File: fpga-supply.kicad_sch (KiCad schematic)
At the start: 70 parts, among them U1 MPFS250T-FCVG484, Y3 Oscillator_125MHz_DSC1103DI2, Y5 Oscillator_50MHz_ECS_1612MV

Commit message: [#57505] Start reworking schematic to hierarchical structure
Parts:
- removed C2, C4: C_100n_0402, antmicro-footprints:C_0402_1005Metric, symbol antmicroCapacitors0402:C_100n_0402
- removed R60, R87: R_0R_0402, antmicro-footprints:R_0402_1005Metric, symbol antmicroResistors0402:R_0R_0402
- removed unit 2 of U1
- removed unit 1 of U1
- removed Y3: Oscillator_125MHz_DSC1103DI2, antmicro-footprints:Oscillator_SMD_Microchip_DSC1103DI2_2.5x2x0.85mm, symbol antmicroOscillators:Oscillator_125MHz_DSC1103DI2
- removed Y5: Oscillator_50MHz_ECS_1612MV, antmicro-footprints:Oscillator_SMD_ECS_1612MV_1.6x1.2x0.6mm, symbol antmicroOscillators:Oscillator_50MHz_ECS_1612MV
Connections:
- no-connect marks 49 -> 0
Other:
- note removed: "2-lane CSI works only when VDDI = 1V8"
- note removed: "PolarFire Bank 0 HSIO"
- note removed: "PolarFire Bank 1 GPIO"
- note removed: "PolarFire clocks"

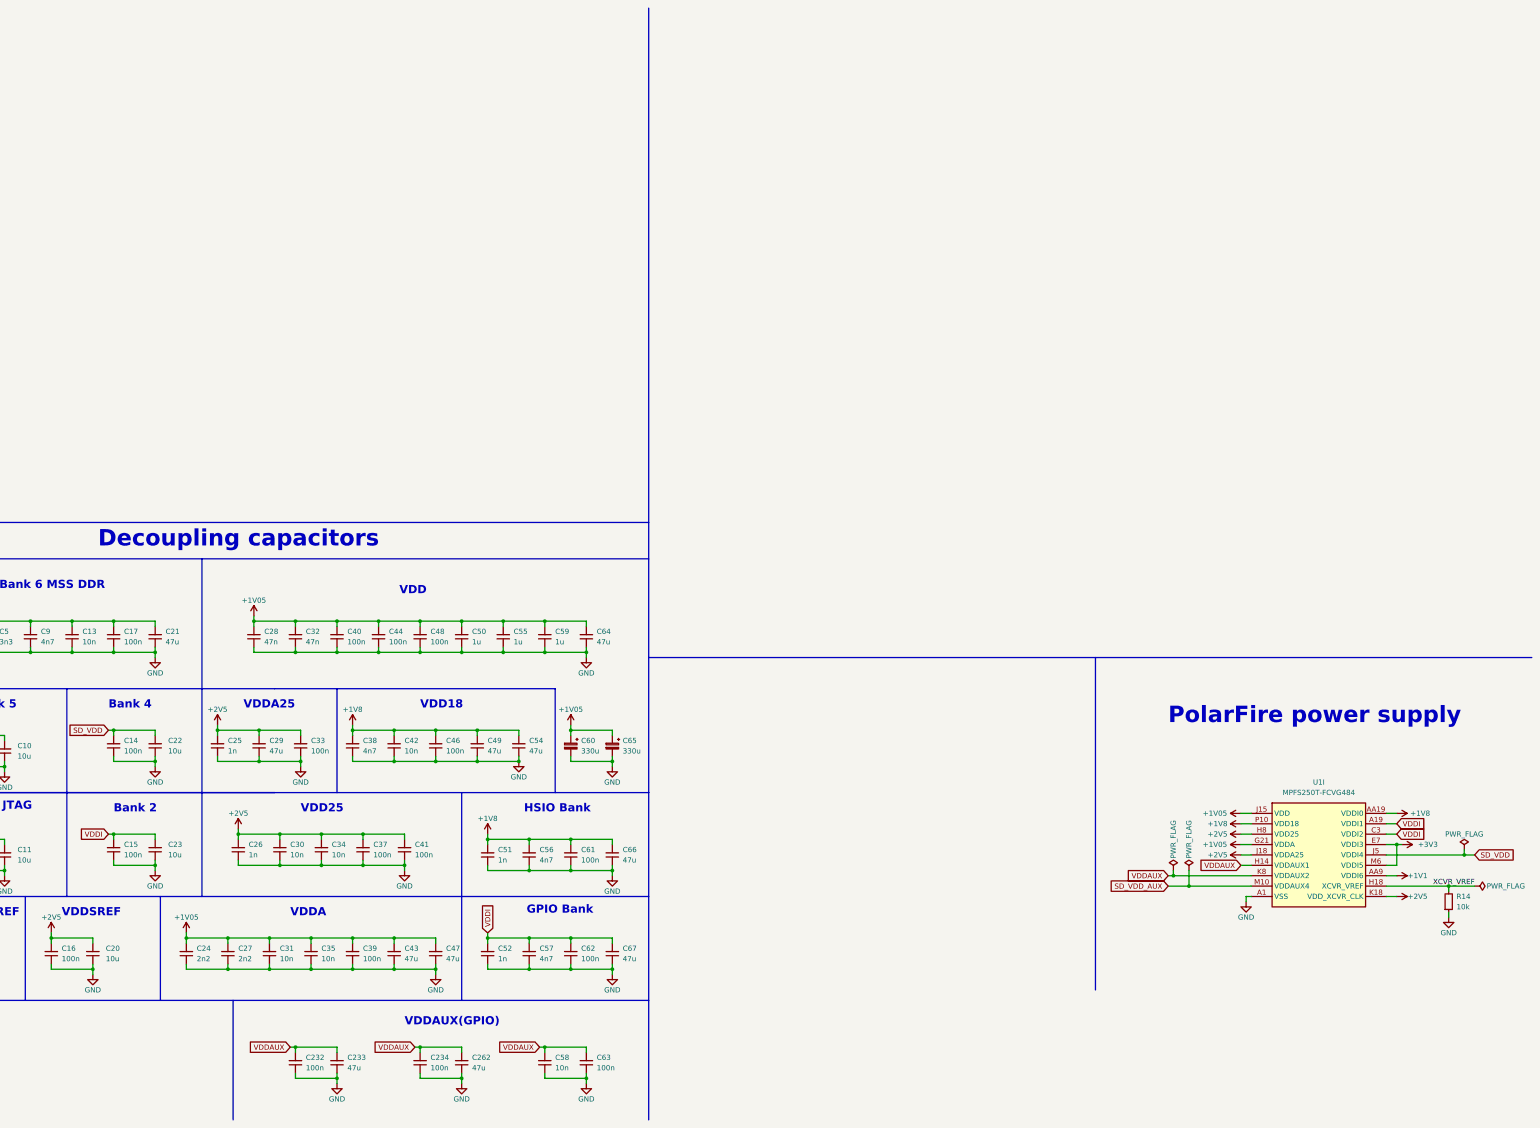
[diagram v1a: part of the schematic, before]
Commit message: [#57505] Continue migration to hierarchical schematic
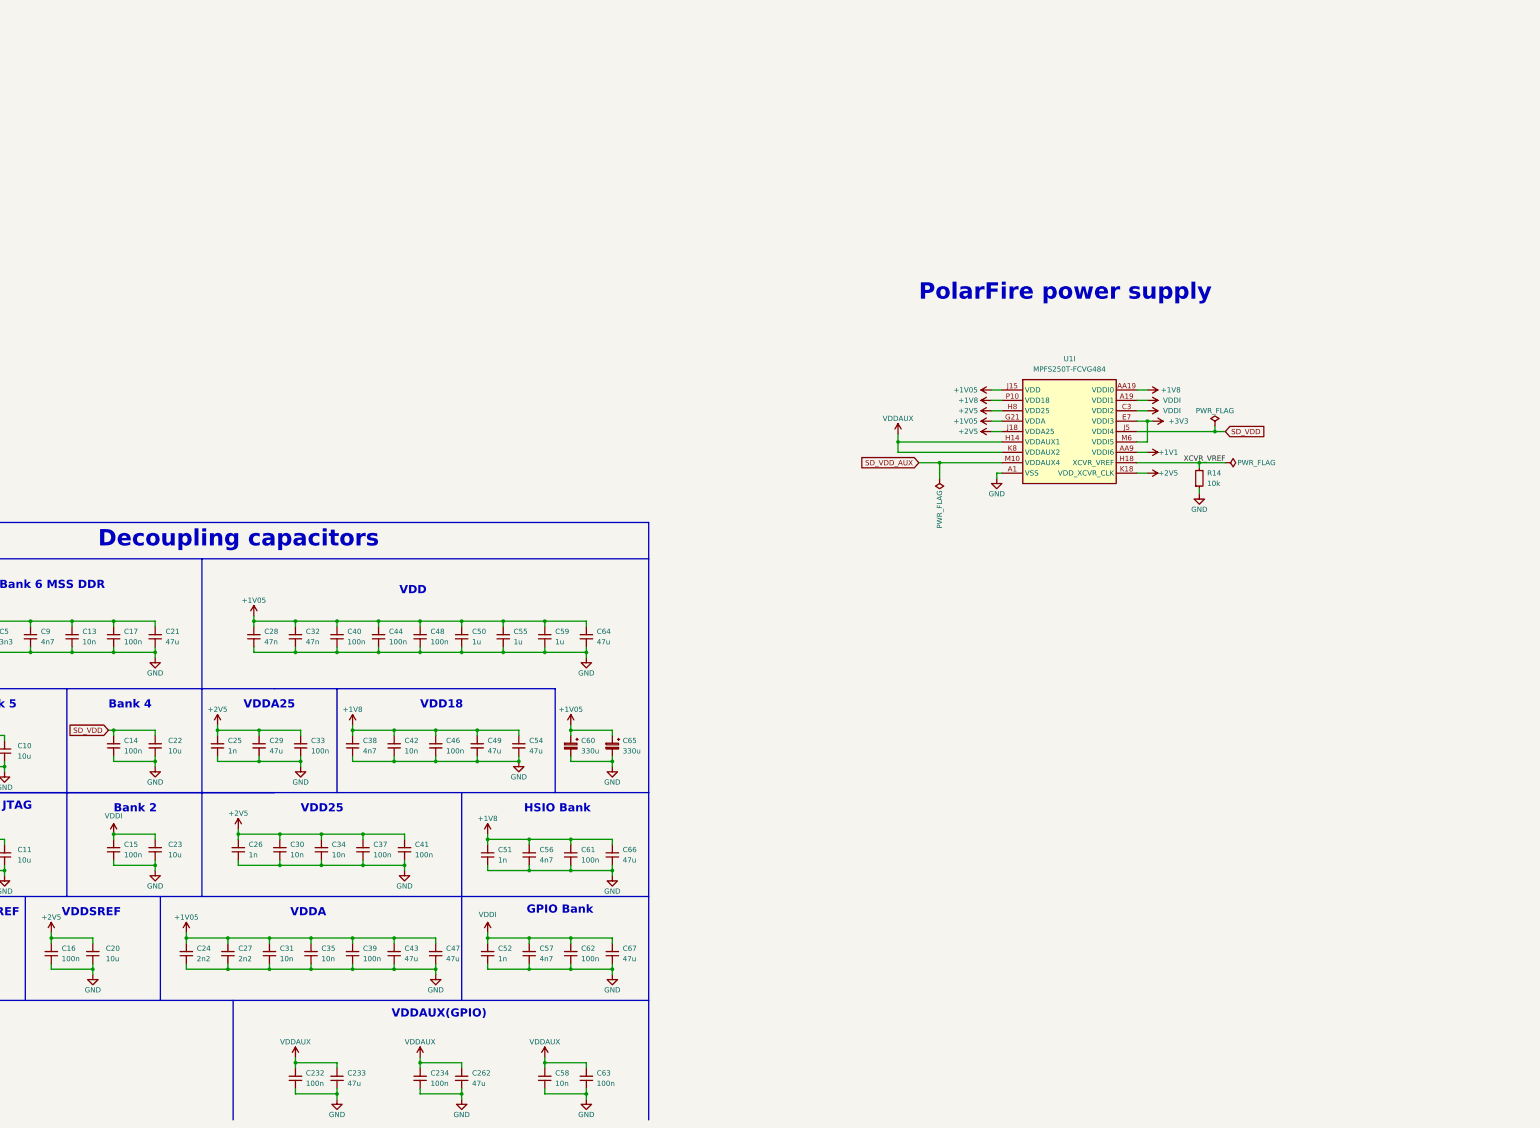
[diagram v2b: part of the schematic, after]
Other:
- moved on the sheet: C232, C233, C234, C262, C58, C63, R14, U1I

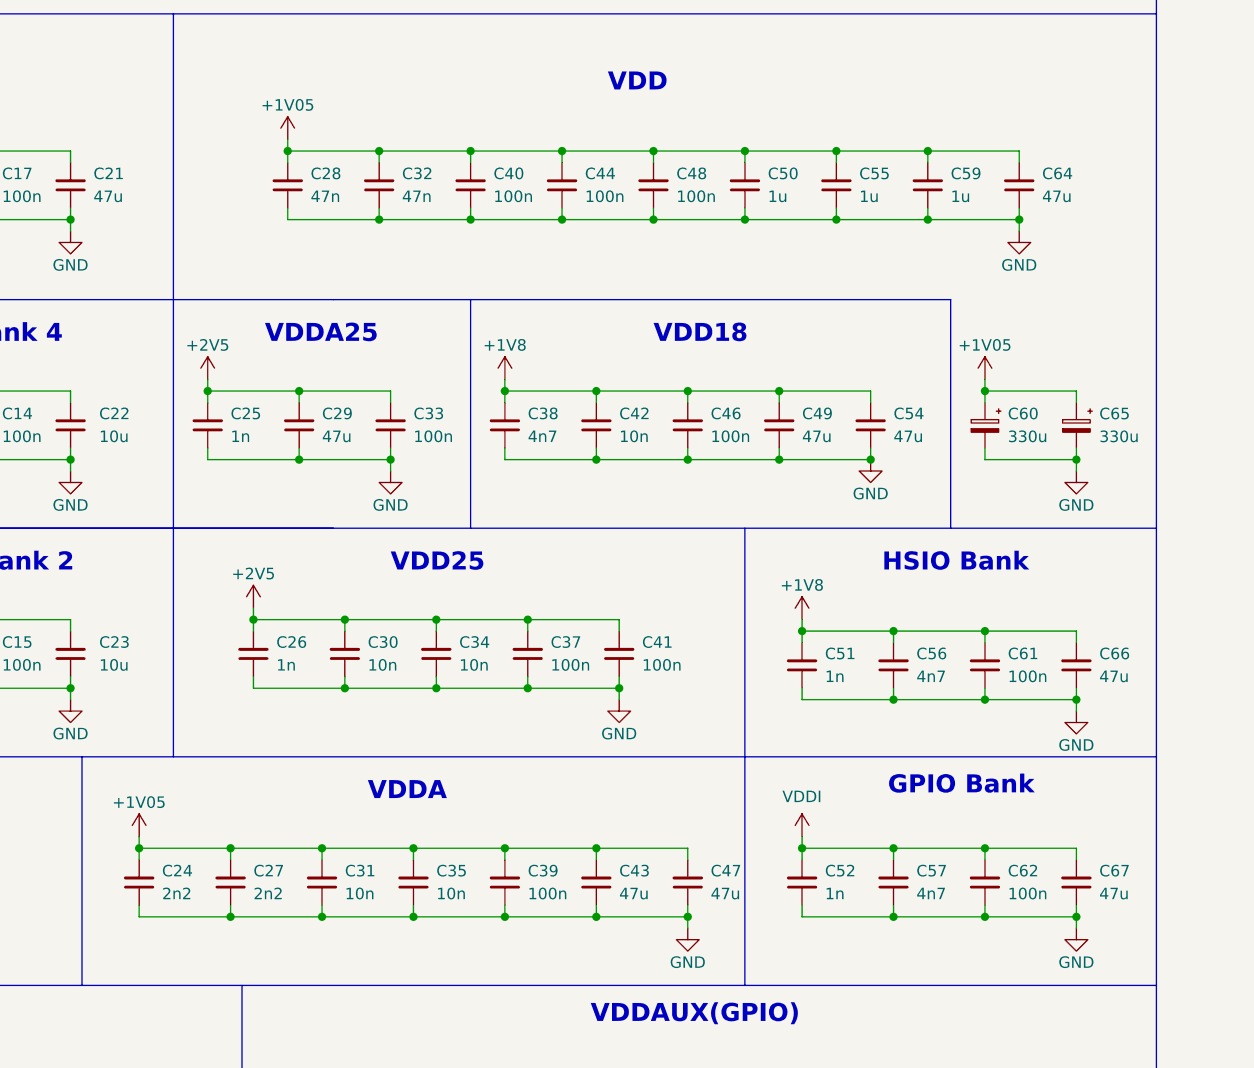
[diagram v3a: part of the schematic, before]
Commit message: [#57422] Update capacitor values
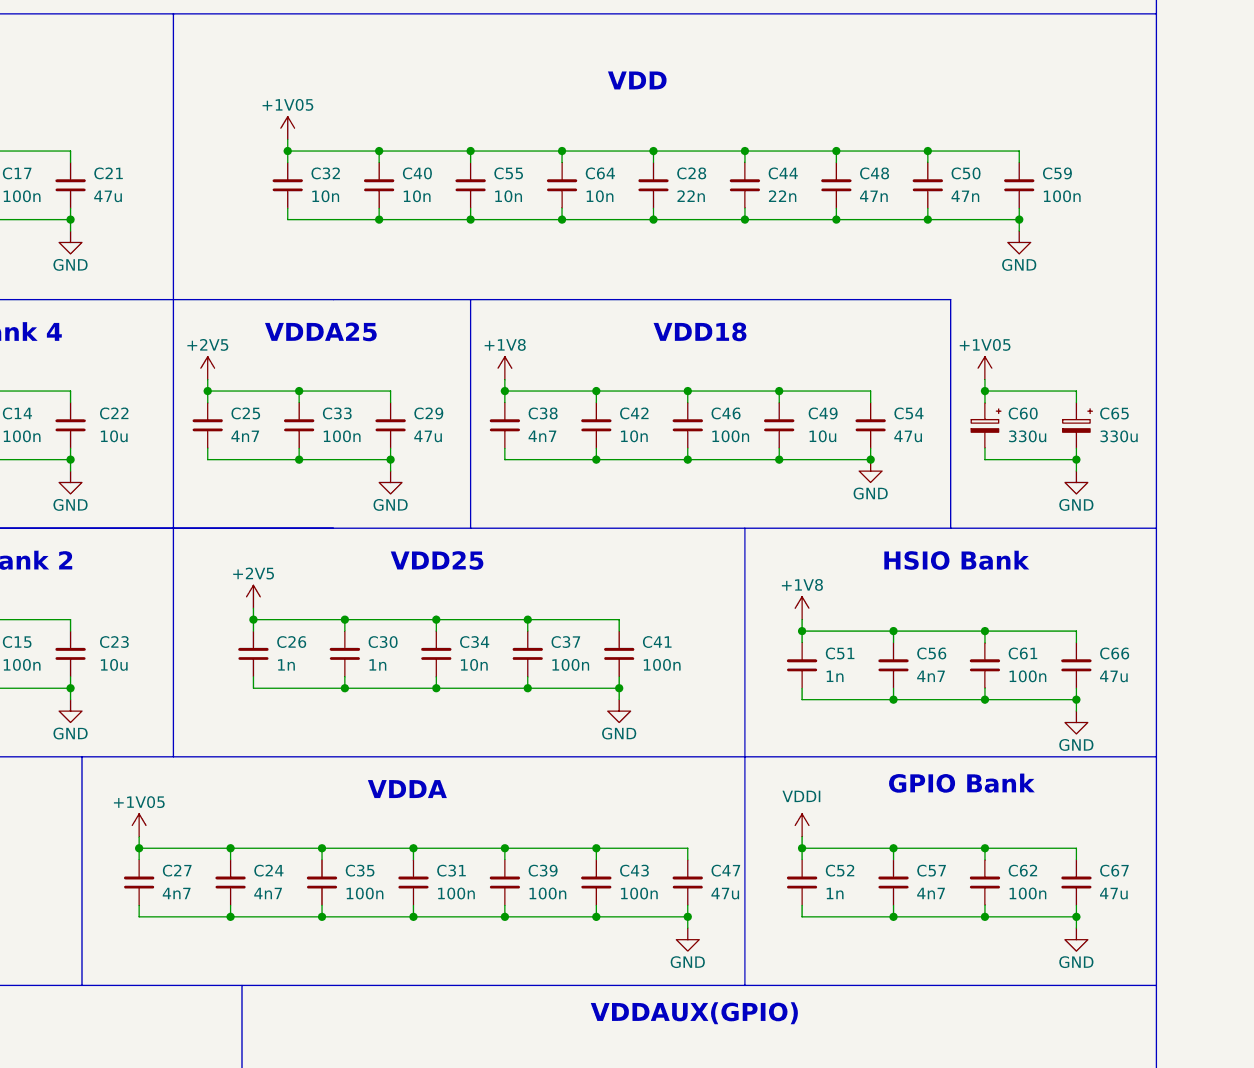
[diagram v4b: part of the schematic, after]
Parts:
- removed C24, C27: C_2n2_0402, antmicro-footprints:C_0402_1005Metric, symbol antmicroCapacitors0402:C_2n2_0402
- removed C25: C_1n_0402, antmicro-footprints:C_0402_1005Metric, symbol antmicroCapacitors0402:C_1n_0402
- removed C28, C32: C_47n_0402, antmicro-footprints:C_0402_1005Metric, symbol antmicroCapacitors0402:C_47n_0402
- removed C30, C31, C35: C_10n_0402, antmicro-footprints:C_0402_1005Metric, symbol antmicroCapacitors0402:C_10n_0402
- removed C40, C44, C48: C_100n_0402, antmicro-footprints:C_0402_1005Metric, symbol antmicroCapacitors0402:C_100n_0402
- removed C43, C49, C64: C_47u_0603, antmicro-footprints:C_0603_1608Metric, symbol antmicroCapacitors0603:C_47u_0603
- removed C50, C55, C59: C_1u_0402, antmicro-footprints:C_0402_1005Metric, symbol antmicroCapacitors0402:C_1u_0402
- added C24, C25, C27: C_4n7_0402, antmicro-footprints:C_0402_1005Metric, symbol antmicroCapacitors0402:C_4n7_0402
- added C28, C44: C_22n_0402, antmicro-footprints:C_0402_1005Metric, symbol antmicroCapacitors0402:C_22n_0402
- added C30: C_1n_0402, antmicro-footprints:C_0402_1005Metric, symbol antmicroCapacitors0402:C_1n_0402
- added C31, C35, C43, C59: C_100n_0402, antmicro-footprints:C_0402_1005Metric, symbol antmicroCapacitors0402:C_100n_0402
- added C32, C40, C55, C64: C_10n_0402, antmicro-footprints:C_0402_1005Metric, symbol antmicroCapacitors0402:C_10n_0402
- added C48, C50: C_47n_0402, antmicro-footprints:C_0402_1005Metric, symbol antmicroCapacitors0402:C_47n_0402
- added C49: C_10u_0402, antmicro-footprints:C_0402_1005Metric, symbol antmicroCapacitors0402:C_10u_0402
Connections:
- net +1V05: now also C24.2, C27.2, C28.2, C31.2, C32.2, C35.2, C40.2, C43.2, C44.2, C48.2, C50.2, C55.2, C59.2, C64.2
- net +1V8: now also C49.2
- net +2V5: now also C25.2, C30.2
- net GND: now also C24.1, C25.1, C27.1, C28.1, C30.1, C31.1, C32.1, C35.1, C40.1, C43.1, C44.1, C48.1, C49.1, C50.1, C55.1, C59.1, C64.1

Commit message: [#57422] Finishing touches
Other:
- moved on the sheet: R14, U1I
